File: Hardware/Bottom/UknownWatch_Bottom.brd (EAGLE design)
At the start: 33 x 33 mm, 32 parts

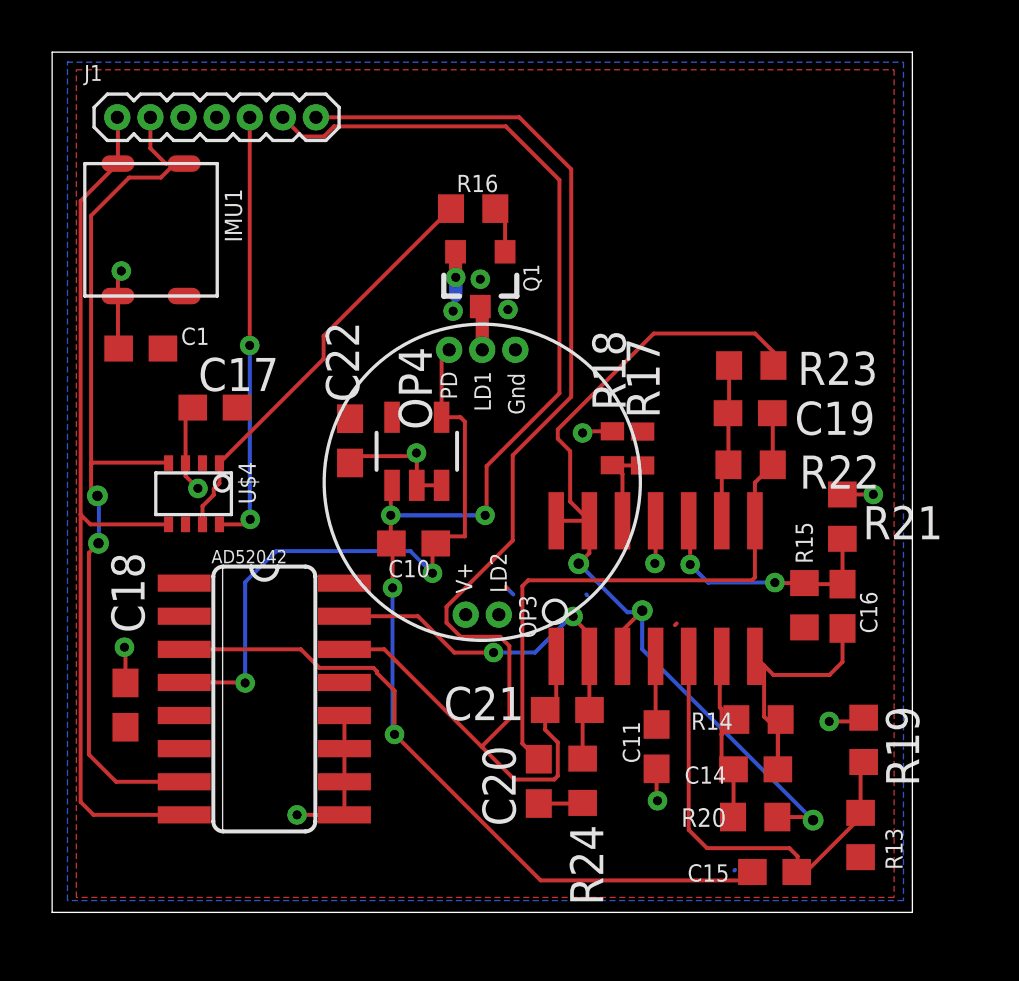
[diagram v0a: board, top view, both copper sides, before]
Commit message: Finshed routing the bottom board except for airwire errors
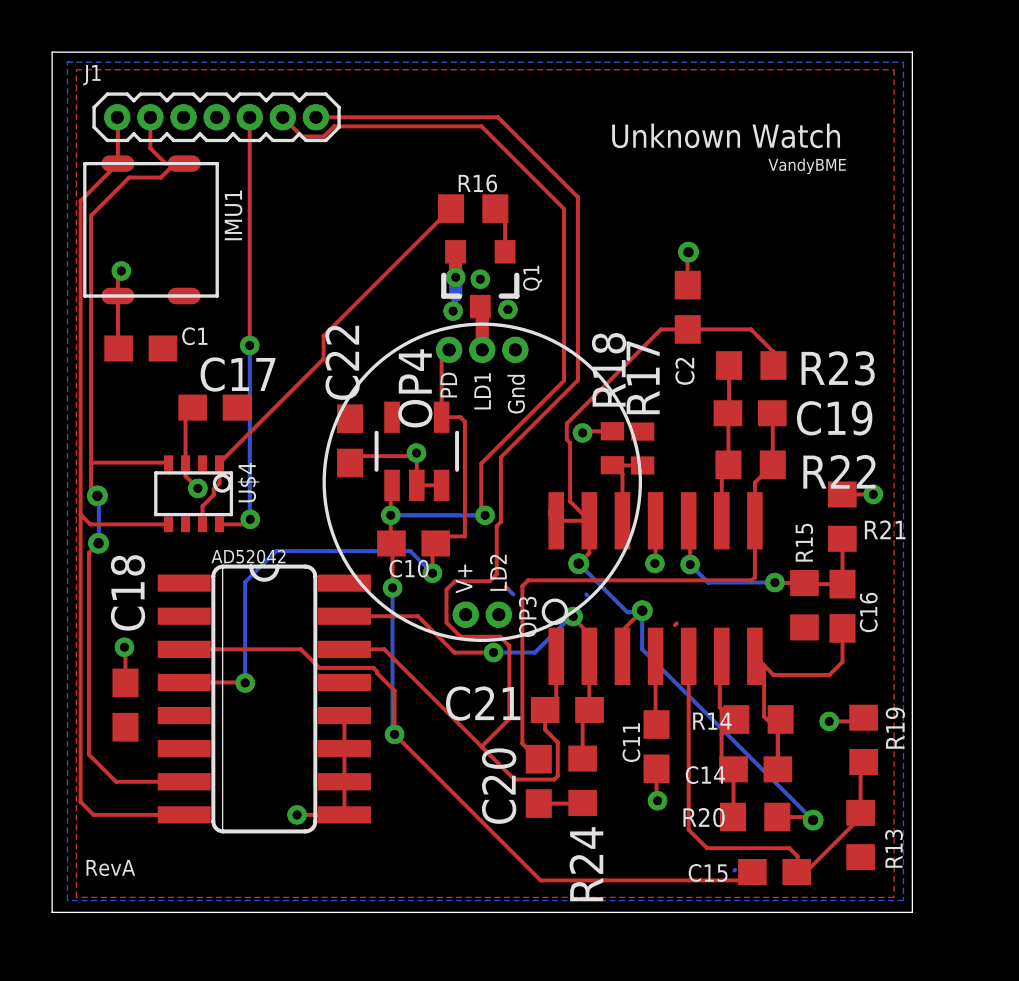
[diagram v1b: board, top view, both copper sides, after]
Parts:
- added C2: 100n, LinnesLab-Passives:C0603
- added U$1: (no value), LinnesLab-Logos:REV.A
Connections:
- net GND: now also C2.1
- net VREF: now also C2.2
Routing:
- net GND: track 26.6 -> 27.9 mm, vias 14 -> 15
- net A7/PPG: track 52.4 -> 52.9 mm
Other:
- board text added: "Unknown Watch"
- board text added: "VandyBME"

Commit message: Completed take 5 and did part of take 6.
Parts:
- added C3, C5, C6: 1u, LinnesLab-Passives:C0603
- added C4, C7: 4.7u, LinnesLab-Passives:C0603
- added CHRG2: MCP73831, LinnesLab-Power:SOT23-5
- added LDO2: MIC5504, LinnesLab-Power:SOT23-5
- added R11: (no value), LinnesLab-Passives:R0603
- added R12: 100k, LinnesLab-Passives:R0603
- added U4: PCF8523, LinnesLab-Clocks:SO8
- added XTAL2: 32.7680kHz, LinnesLab-Clocks:2-SMD.NOLEAD.2.0MMTO1.2MM
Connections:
- new net D27/CHRG.STATUS: CHRG2.1, R12.1
- new net N$1: U4.1, XTAL2.P$2
- new net N$2: CHRG2.5, R11.2
- new net N$6: U4.2, XTAL2.P$1
- new net VBAT: U4.3
- new net VIN: C5.2, C7.2, CHRG2.4, LDO2.1, LDO2.3, R12.2
- new net VLIPO: C4.1, CHRG2.3
- net 3.3V: now also C3.1, C6.1, LDO2.5, U4.8
- net GND: now also C3.2, C4.2, C5.1, C6.2, C7.1, CHRG2.2, LDO2.2, R11.1, U4.4
- net SCL: now also U4.6
- net SDA: now also U4.5
